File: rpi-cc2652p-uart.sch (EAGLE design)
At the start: 10 parts, among them U1 CC2652P2-DUOWEISI, U2 AP2112K

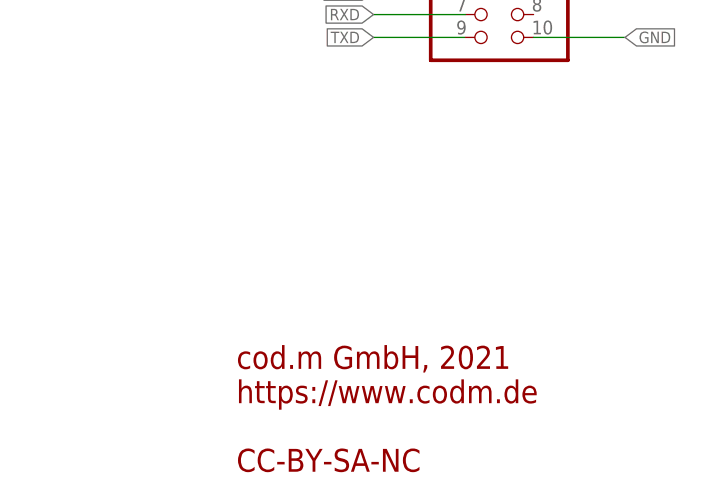
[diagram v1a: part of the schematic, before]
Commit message: 0805 to 0603
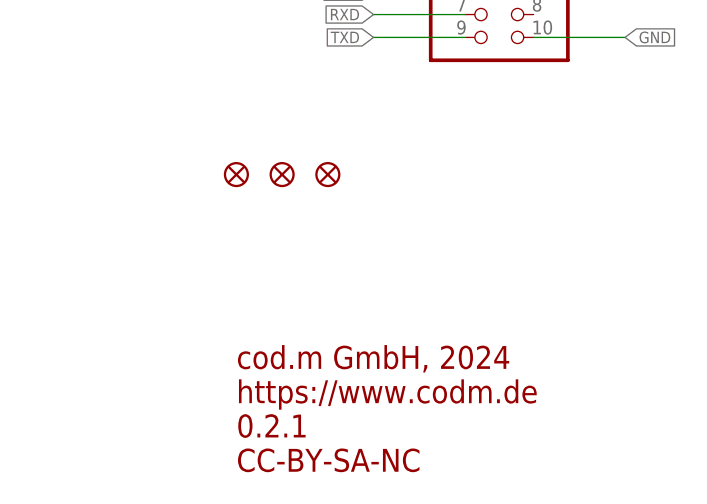
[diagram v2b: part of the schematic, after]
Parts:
- added FD1, FD2, FD3: FIDUCIAL1X2, SparkFun-Aesthetics:FIDUCIAL1X2
- C1: device rcl:C-EUC0805 -> rcl:C-EUC0603K
- R1: device rcl:R-EU_R0805 -> codm:R-EU_R0603RF
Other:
- note added: "cod.m GmbH, 2024 https://www.codm.de 0.2.1 CC-BY-SA-NC"
- note removed: "cod.m GmbH, 2021 https://www.codm.de CC-BY-SA-NC"
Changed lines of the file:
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@@
 <drawing>
 <settings>
-<setting alwaysvectorfont="yes"/>
+<setting alwaysvectorfont="no"/>
 <setting verticaltext="up"/>
 </settings>
@@
 <layer number="56" name="wert" color="7" fill="1" visible="no" active="no"/>
 <layer number="57" name="tCAD" color="7" fill="1" visible="no" active="no"/>
+<layer number="58" name="bCAD" color="7" fill="1" visible="no" active="no"/>
 <layer number="59" name="tCarbon" color="7" fill="1" visible="no" active="no"/>
 <layer number="60" name="bCarbon" color="7" fill="1" visible="no" active="no"/>
@@
 <layer number="131" name="tAdjust" color="7" fill="1" visible="no" active="yes"/>
 <layer number="132" name="bAdjust" color="7" fill="1" visible="no" active="yes"/>
+<layer number="133" name="bottom_silk" color="7" fill="1" visible="no" active="no"/>
+<layer number="134" name="silk_top" color="7" fill="1" visible="no" active="no"/>
+<layer number="135" name="silk_bottom" color="7" fill="1" visible="no" active="no"/>
+<layer number="136" name="silktop" color="7" fill="1" visible="no" active="no"/>
+<layer number="137" name="silkbottom" color="7" fill="1" visible="no" active="no"/>
+<layer number="138" name="EEE" color="7" fill="1" visible="no" active="no"/>
+<layer number="139" name="_tKeepout" color="7" fill="1" visible="no" active="no"/>
+<layer number="140" name="mbKeepout" color="7" fill="1" visible="no" active="no"/>
+<layer number="141" name="ASSEMBLY_TOP" color="7" fill="1" visible="no" active="no"/>
+<layer number="142" name="mbRestrict" color="7" fill="1" visible="no" active="no"/>
+<layer number="143" name="PLACE_BOUND_TOP" color="7" fill="1" visible="no" active="no"/>
 <layer number="144" name="Drill_legend" color="7" fill="1" visible="no" active="no"/>
+<layer number="145" name="DrillLegend_01-16" color="7" fill="1" visible="no" active="no"/>
+<layer number="146" name="DrillLegend_01-20" color="7" fill="1" visible="no" active="no"/>
+<layer number="147" name="PIN_NUMBER" color="7" fill="1" visible="no" active="no"/>
+<layer number="148" name="DrillLegend_01-20" color="7" fill="1" visible="no" active="no"/>
+<layer number="149" name="DrillLegend_02-15" color="7" fill="1" visible="no" active="no"/>
 <layer number="150" name="Notes" color="7" fill="1" visible="no" active="yes"/>
 <layer number="151" name="HeatSink" color="14" fill="1" visible="no" active="no"/>
@@
 <layer number="154" name="FabDoc2" color="2" fill="1" visible="no" active="no"/>
 <layer number="155" name="FabDoc3" color="7" fill="15" visible="no" active="no"/>
+<layer number="166" name="AntennaArea" color="7" fill="1" visible="no" active="no"/>
+<layer number="168" name="4mmHeightArea" color="7" fill="1" visible="no" active="no"/>
+<layer number="191" name="mNets" color="7" fill="1" visible="no" active="no"/>
+<layer number="192" name="mBusses" color="7" fill="1" visible="no" active="no"/>
+<layer number="193" name="mPins" color="7" fill="1" visible="no" active="no"/>
+<layer number="194" name="mSymbols" color="7" fill="1" visible="no" active="no"/>
+<layer number="195" name="mNames" color="7" fill="1" visible="no" active="no"/>
+<layer number="196" name="mValues" color="7" fill="1" visible="no" active="no"/>
 <layer number="199" name="Contour" color="7" fill="1" visible="no" active="yes"/>
 <layer number="200" name="200bmp" color="1" fill="10" visible="yes" active="yes"/>
@@
 <layer number="250" name="Descript" color="3" fill="1" visible="no" active="no"/>
 <layer number="251" name="SMDround" color="12" fill="11" visible="no" active="no"/>
+<layer number="253" name="Extra" color="7" fill="1" visible="no" active="no"/>
 <layer number="254" name="OrgLBR" color="13" fill="1" visible="no" active="no"/>
 <layer number="255" name="routoute" color="7" fill="1" visible="yes" active="yes"/>
@@
 <parts>
 <part name="JP1" library="pinhead" deviceset="PINHD-2X5" device="" override_package3d_urn="urn:adsk.eagle:package:22254121/2" override_package_urn="urn:adsk.eagle:footprint:22254122/1"/>
-<part name="R1" library="rcl" library_urn="urn:adsk.eagle:library:334" deviceset="R-EU_" device="R0805" package3d_urn="urn:adsk.eagle:package:23553/2" value="1k"/>
+<part name="R1" library="codm" library_urn="urn:adsk.eagle:library:11602856" deviceset="R-EU_" device="R0603RF" package3d_urn="urn:adsk.eagle:package:11602922/5" value="1k"/>
 <part name="JTAG" library="20021121-00010C4LF" deviceset="20021121-00010C4LF" device="" override_package3d_urn="urn:adsk.eagle:package:22254096/2" override_package_urn="urn:adsk.eagle:footprint:22254097/1"/>
 <part name="RESET" library="434153017835_Eagle_WS-TASV_rev20a" deviceset="434153017835" device="" package3d_urn="urn:adsk.eagle:package:18304352/2"/>
@@
 <part name="P+3" library="supply1" library_urn="urn:adsk.eagle:library:371" deviceset="+5V" device=""/>
 <part name="P+4" library="supply1" library_urn="urn:adsk.eagle:library:371" deviceset="VCC" device=""/>
-<part name="C1" library="rcl" library_urn="urn:adsk.eagle:library:334" deviceset="C-EU" device="C0805" package3d_urn="urn:adsk.eagle:package:23617/2" value="100n"/>
+<part name="C1" library="rcl" library_urn="urn:adsk.eagle:library:334" deviceset="C-EU" device="C0603K" package3d_urn="urn:adsk.eagle:package:23680/2" value="100n"/>
+<part name="FD1" library="SparkFun-Aesthetics" library_urn="urn:adsk.eagle:library:507" deviceset="FIDUCIAL" device="1X2" package3d_urn="urn:adsk.eagle:package:41384560/3"/>
+<part name="FD2" library="SparkFun-Aesthetics" library_urn="urn:adsk.eagle:library:507" deviceset="FIDUCIAL" device="1X2" package3d_urn="urn:adsk.eagle:package:41384560/3"/>
+<part name="FD3" library="SparkFun-Aesthetics" library_urn="urn:adsk.eagle:library:507" deviceset="FIDUCIAL" device="1X2" package3d_urn="urn:adsk.eagle:package:41384560/3"/>
 </parts>
 <sheets>
 <sheet>
 <plain>
-<text x="185.42" y="-5.08" size="2.54" layer="94">cod.m GmbH, 2021
+<text x="185.42" y="-5.08" size="2.54" layer="94">cod.m GmbH, 2024
 https://www.codm.de
+0.2.1
 CC-BY-SA-NC</text>
 </plain>
@@
 <attribute name="VALUE" x="92.456" y="73.279" size="1.778" layer="96" rot="R180"/>
 </instance>
+<instance part="FD1" gate="G$1" x="185.42" y="27.94" smashed="yes"/>
+<instance part="FD2" gate="G$1" x="190.5" y="27.94" smashed="yes"/>
+<instance part="FD3" gate="G$1" x="195.58" y="27.94" smashed="yes"/>
 </instances>
 <busses>
@@
 will not be understood (or retained) with this version.
 </note>
-<note version="8.4" severity="warning">
-Since Version 8.4, EAGLE supports properties for SPICE simulation.
-Probes in schematics and SPICE mapping objects found in parts and library devices
-will not be understood with this version. Update EAGLE to the latest version
-for full support of SPICE simulation.
-</note>
 </compatibility>
